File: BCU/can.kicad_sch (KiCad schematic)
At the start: 7 parts

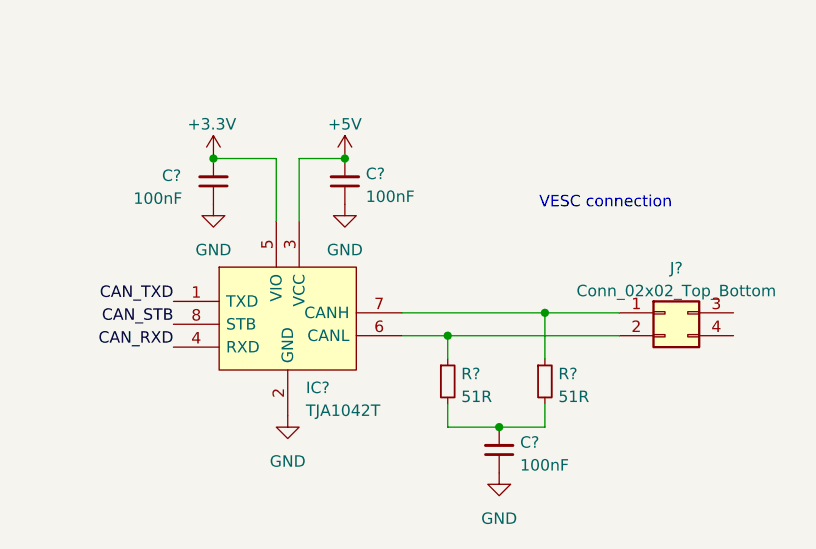
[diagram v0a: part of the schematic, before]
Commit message: Make rough component placement for evaluating missing 3D
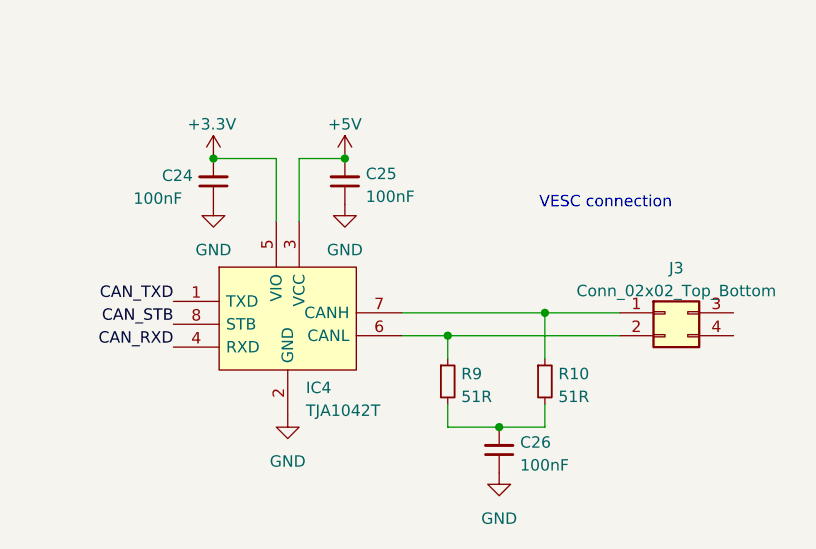
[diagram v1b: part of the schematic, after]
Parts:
- gave numbers to parts that had none: 7
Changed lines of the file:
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@@
   (symbol (lib_id "power:+5V") (at 106.68 66.675 0) (unit 1)
     (in_bom yes) (on_board yes)
-    (property "Reference" "#PWR?" (id 0) (at 106.68 70.485 0)
+    (property "Reference" "#PWR0144" (id 0) (at 106.68 70.485 0)
       (effects (font (size 1.27 1.27)) hide)
     )
@@
   (symbol (lib_id "Device:C_Small") (at 92.075 69.215 180) (unit 1)
     (in_bom yes) (on_board yes)
-    (property "Reference" "C?" (id 0) (at 86.36 68.58 0)
+    (property "Reference" "C24" (id 0) (at 86.36 68.58 0)
       (effects (font (size 1.27 1.27)) (justify right))
     )
@@
   (symbol (lib_id "coilchain-com:TJA1042T") (at 87.63 82.55 0) (unit 1)
     (in_bom yes) (on_board yes) (fields_autoplaced)
-    (property "Reference" "IC?" (id 0) (at 102.3494 92.1496 0)
+    (property "Reference" "IC4" (id 0) (at 102.3494 92.1496 0)
       (effects (font (size 1.27 1.27)) (justify left))
     )
@@
   (symbol (lib_id "Connector_Generic:Conn_02x02_Top_Bottom") (at 142.24 83.82 0) (unit 1)
     (in_bom yes) (on_board yes) (fields_autoplaced)
-    (property "Reference" "J?" (id 0) (at 143.51 78.8502 0))
+    (property "Reference" "J3" (id 0) (at 143.51 78.8502 0))
     (property "Value" "Conn_02x02_Top_Bottom" (id 1) (at 143.51 81.3871 0))
     (property "Footprint" "" (id 2) (at 142.24 83.82 0)
@@
   (symbol (lib_id "power:GND") (at 100.33 95.25 0) (unit 1)
     (in_bom yes) (on_board yes) (fields_autoplaced)
-    (property "Reference" "#PWR?" (id 0) (at 100.33 101.6 0)
+    (property "Reference" "#PWR0148" (id 0) (at 100.33 101.6 0)
       (effects (font (size 1.27 1.27)) hide)
     )
@@
   (symbol (lib_id "power:+3.3V") (at 92.075 66.675 0) (unit 1)
     (in_bom yes) (on_board yes)
-    (property "Reference" "#PWR?" (id 0) (at 92.075 70.485 0)
+    (property "Reference" "#PWR0145" (id 0) (at 92.075 70.485 0)
       (effects (font (size 1.27 1.27)) hide)
     )
@@
   (symbol (lib_id "Device:R_Small") (at 118.11 91.44 0) (unit 1)
     (in_bom yes) (on_board yes) (fields_autoplaced)
-    (property "Reference" "R?" (id 0) (at 119.6086 90.6053 0)
+    (property "Reference" "R9" (id 0) (at 119.6086 90.6053 0)
       (effects (font (size 1.27 1.27)) (justify left))
     )
@@
   (symbol (lib_id "power:GND") (at 92.075 71.755 0) (unit 1)
     (in_bom yes) (on_board yes) (fields_autoplaced)
-    (property "Reference" "#PWR?" (id 0) (at 92.075 78.105 0)
+    (property "Reference" "#PWR0146" (id 0) (at 92.075 78.105 0)
       (effects (font (size 1.27 1.27)) hide)
     )
@@
   (symbol (lib_id "Device:R_Small") (at 128.905 91.44 0) (unit 1)
     (in_bom yes) (on_board yes) (fields_autoplaced)
-    (property "Reference" "R?" (id 0) (at 130.4036 90.6053 0)
+    (property "Reference" "R10" (id 0) (at 130.4036 90.6053 0)
       (effects (font (size 1.27 1.27)) (justify left))
     )
@@
   (symbol (lib_id "power:GND") (at 106.68 71.755 0) (unit 1)
     (in_bom yes) (on_board yes) (fields_autoplaced)
-    (property "Reference" "#PWR?" (id 0) (at 106.68 78.105 0)
+    (property "Reference" "#PWR0149" (id 0) (at 106.68 78.105 0)
       (effects (font (size 1.27 1.27)) hide)
     )
@@
   (symbol (lib_id "power:GND") (at 123.825 101.6 0) (unit 1)
     (in_bom yes) (on_board yes) (fields_autoplaced)
-    (property "Reference" "#PWR?" (id 0) (at 123.825 107.95 0)
+    (property "Reference" "#PWR0147" (id 0) (at 123.825 107.95 0)
       (effects (font (size 1.27 1.27)) hide)
     )
@@
   (symbol (lib_id "Device:C_Small") (at 123.825 99.06 180) (unit 1)
     (in_bom yes) (on_board yes) (fields_autoplaced)
-    (property "Reference" "C?" (id 0) (at 126.1491 98.2189 0)
+    (property "Reference" "C26" (id 0) (at 126.1491 98.2189 0)
       (effects (font (size 1.27 1.27)) (justify right))
     )
@@
   (symbol (lib_id "Device:C_Small") (at 106.68 69.215 180) (unit 1)
     (in_bom yes) (on_board yes) (fields_autoplaced)
-    (property "Reference" "C?" (id 0) (at 109.0041 68.3739 0)
-      (effects (font (size 1.27 1.27)) (justify right))
-    )
+    (property "Reference" "C25" (id 0) (at 109.0041 68.3739 0)
+      (effects (font (size 1.27 1.27)) (justify right))
+    )
